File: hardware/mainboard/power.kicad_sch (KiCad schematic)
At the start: 17 parts, among them J105 Eurorack_Power, U1 LM4040DBZ-10, U2 XX1117-3.3

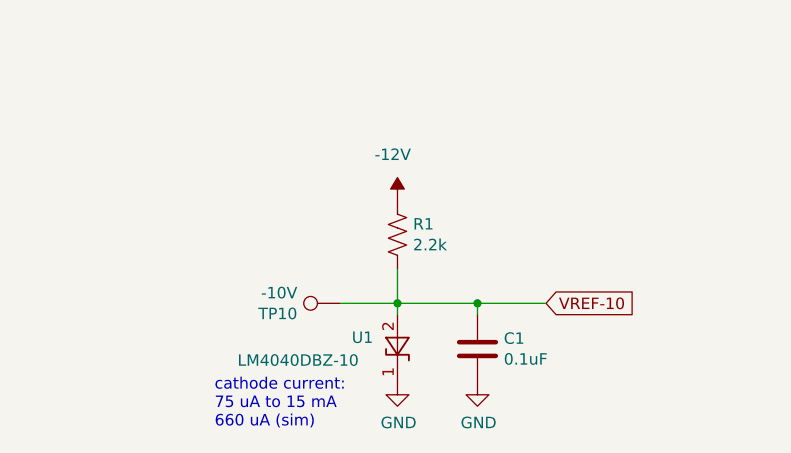
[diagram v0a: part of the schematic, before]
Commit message: Get DRC passing
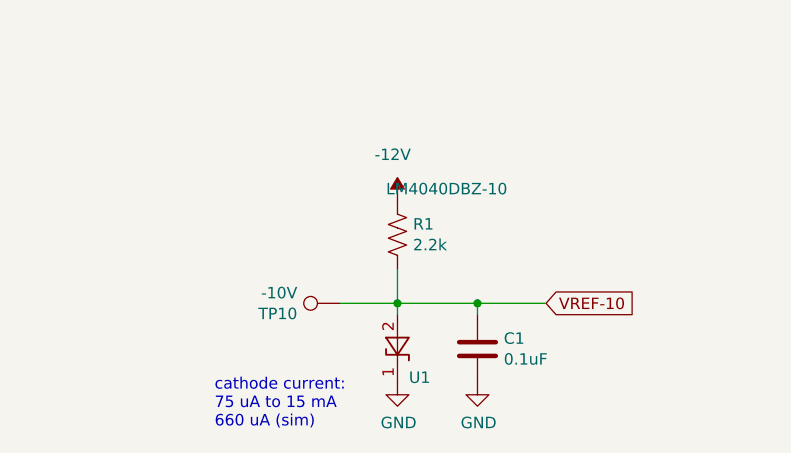
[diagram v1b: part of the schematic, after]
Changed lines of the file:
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@@
   (symbol (lib_id "Reference_Voltage:LM4040DBZ-10") (at 55.88 83.82 270) (unit 1)
     (in_bom yes) (on_board yes)
-    (property "Reference" "U1" (id 0) (at 50.8 82.55 90)
+    (property "Reference" "U1" (id 0) (at 57.15 86.995 90)
       (effects (font (size 1.27 1.27)) (justify left))
     )
-    (property "Value" "LM4040DBZ-10" (id 1) (at 38.1 85.09 90)
+    (property "Value" "LM4040DBZ-10" (id 1) (at 54.61 66.04 90)
       (effects (font (size 1.27 1.27)) (justify left))
     )
-    (property "Footprint" "Package_TO_SOT_SMD:SOT-23" (id 2) (at 50.8 83.82 0)
+    (property "Footprint" "Package_TO_SOT_SMD:SOT-23" (id 2) (at 55.88 78.74 0)
       (effects (font (size 1.27 1.27) italic) hide)
     )
@@
       (effects (font (size 1.27 1.27)) hide)
     )
+    (pin "3")
     (pin "1")
     (pin "2")

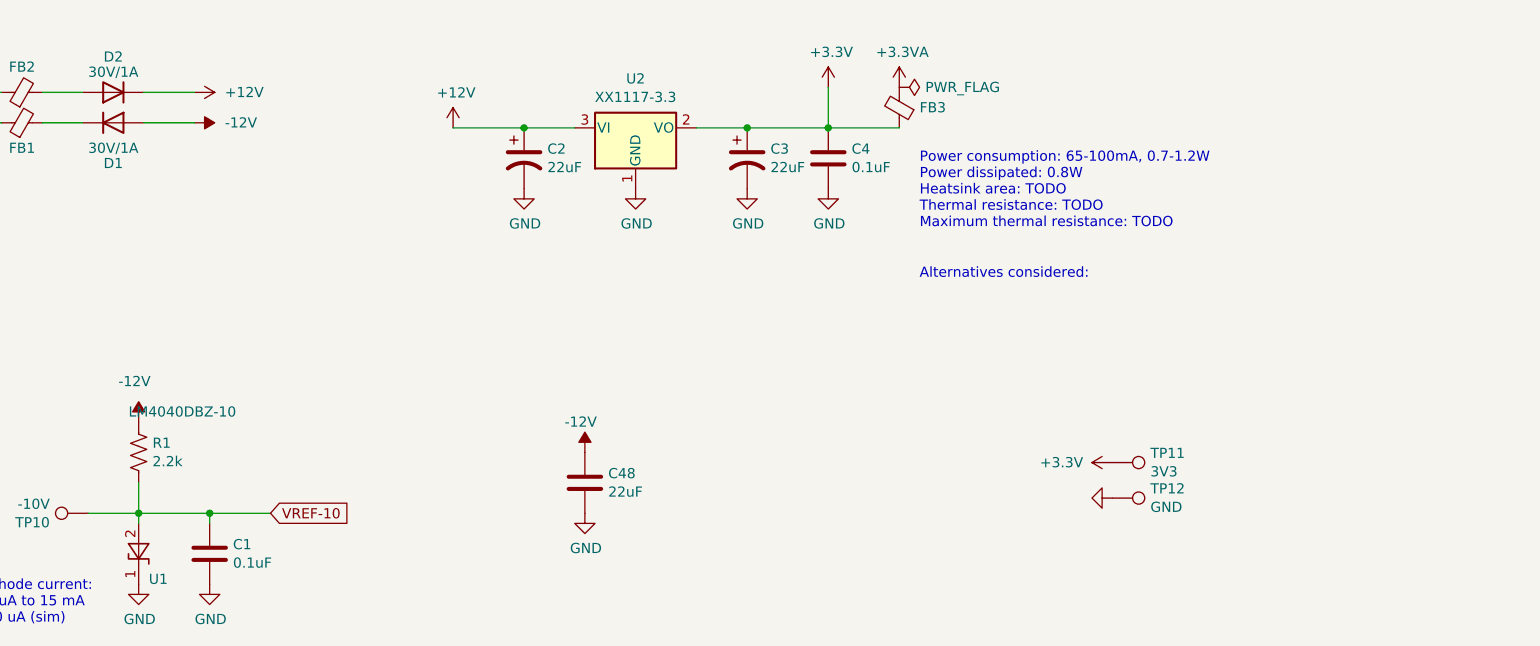
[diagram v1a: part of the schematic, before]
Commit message: Add ESD protection for inputs
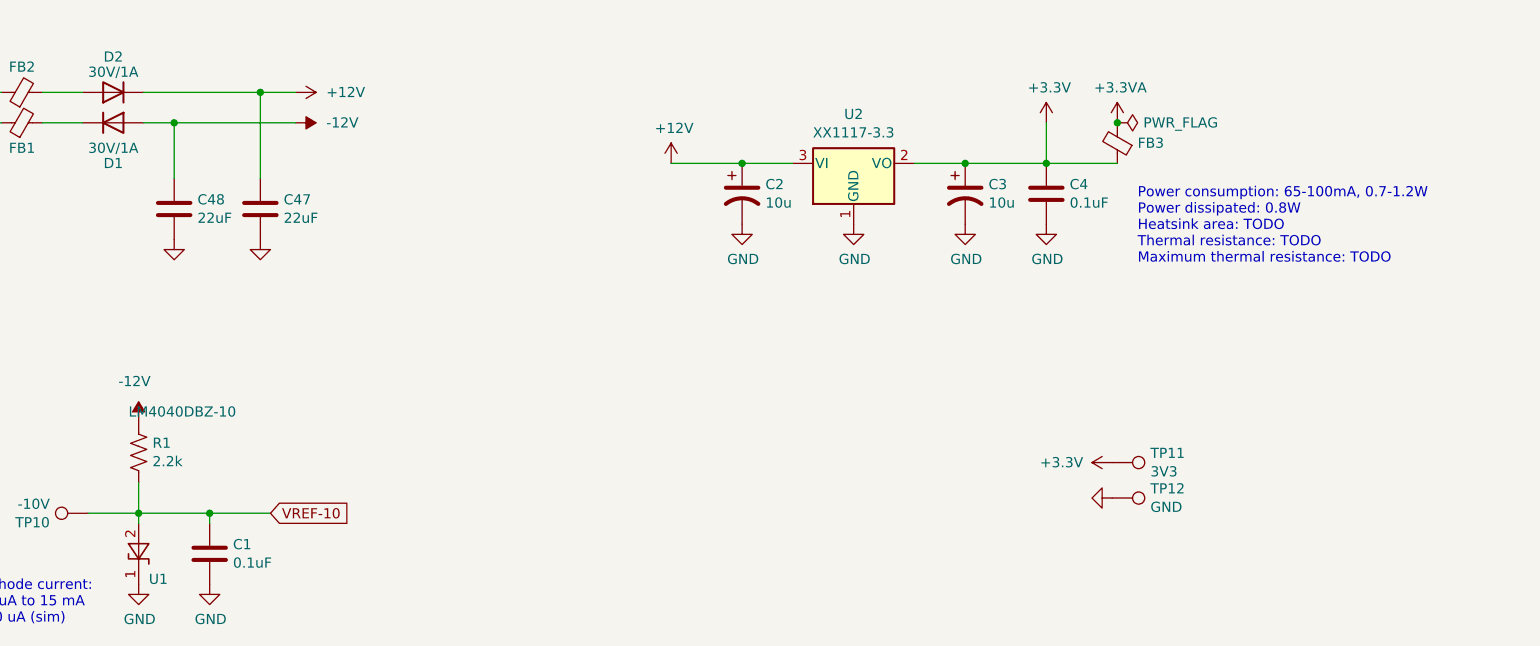
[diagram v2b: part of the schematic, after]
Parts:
- added C47: 22uF, Capacitor_SMD:C_0805_2012Metric_Pad1.18x1.45mm_HandSolder, symbol Device:C
- C2, C3: value 22uF -> 10u; mpn CL21A226MOQNNNE -> (none)
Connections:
- net +12V: now also C47.1
- net GND: now also C47.2
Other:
- note removed: "Alternatives considered:"
- moved on the sheet: C2, C3, C4, C48, FB3, U2

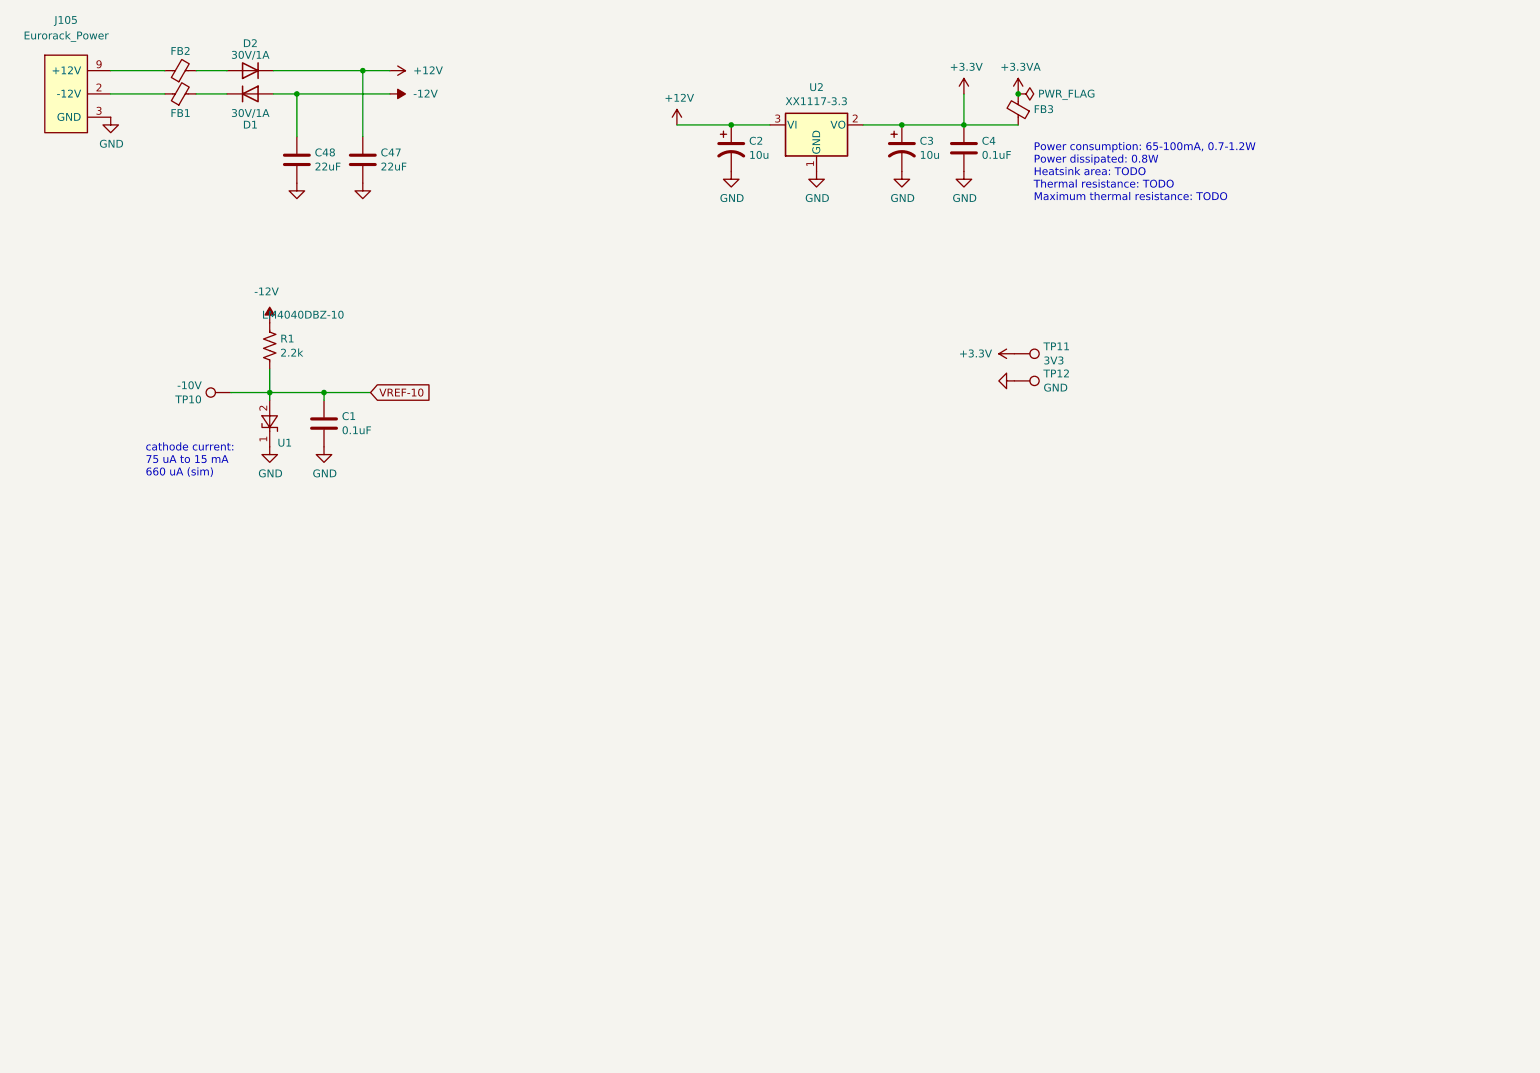
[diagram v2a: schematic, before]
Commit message: Progress on cleaning up the schematics
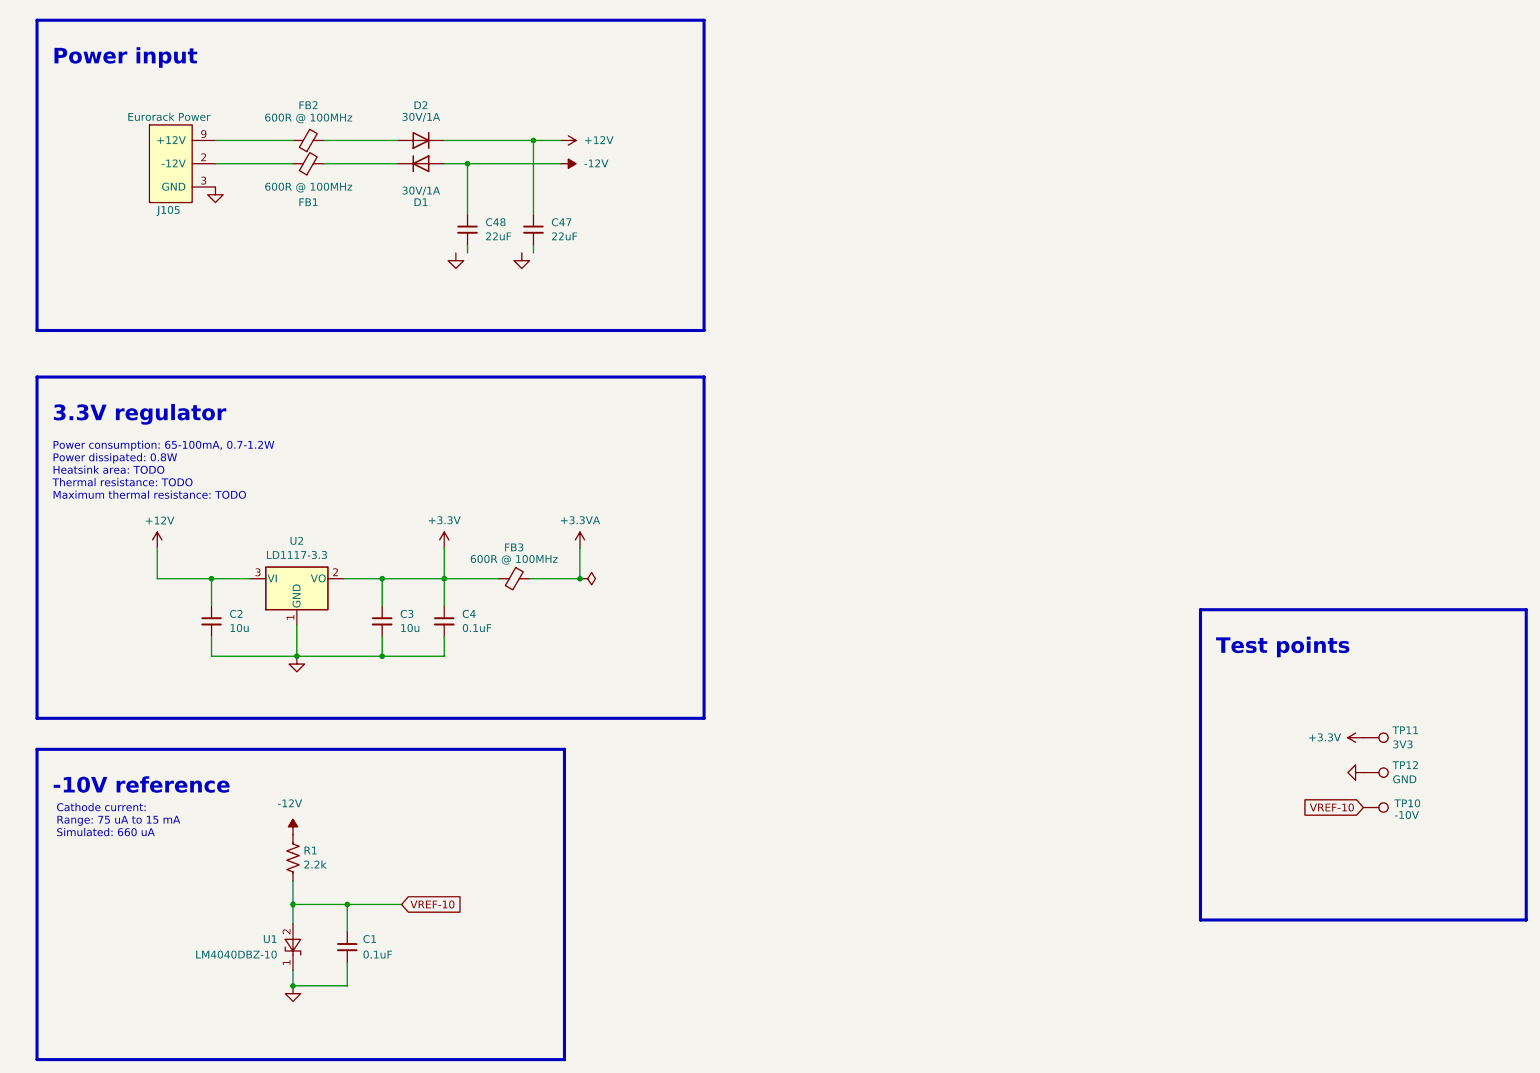
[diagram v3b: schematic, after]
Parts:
- C1, C4, C47, C48: symbol Device:C -> Device:C_Small
- C2, C3: symbol Device:C_Polarized_US -> Device:C_Small
- FB1, FB2: value Ferrite Bead -> 600R @ 100MHz
- FB3: value Ferrite Bead -> 600R @ 100MHz; Reqs >500mA DC current -> >200mA DC current
- J105: value Eurorack_Power -> Eurorack Power
- U2: value XX1117-3.3 -> LD1117-3.3
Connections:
- net +3.3VA: now also FB3.1; no longer FB3.2
- net +3V3: now also FB3.2; no longer FB3.1
- net GND: no longer C47.2, C48.2
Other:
- note added: "-10V reference"
- note added: "3.3V regulator"
- note added: "Cathode current: Range: 75 uA to 15 mA Simulated: 660 uA"
- note added: "Power input"
- note added: "Test points"
- note removed: "cathode current: 75 uA to 15 mA 660 uA (sim)"
- moved on the sheet: C1, C4, C47, C48, D1, D2, FB1, FB2, FB3, J105, R1, TP10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

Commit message: Fixup some wacked stuff from the schematic cleanup
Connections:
- net +3.3VA: now also FB3.2; no longer FB3.1
- net +3V3: now also FB3.1; no longer FB3.2
- net GND: now also C47.2, C48.2
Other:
- moved on the sheet: FB3
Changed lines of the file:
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@@
     (pin "2")
   )
-  (symbol (lib_id "Device:FerriteBead_Small") (at 95.885 109.22 270) (unit 1)
+  (symbol (lib_id "Device:FerriteBead_Small") (at 95.885 109.22 90) (unit 1)
     (in_bom yes) (on_board yes)
     (property "Reference" "FB3" (id 0) (at 95.885 104.14 90))
     (property "Value" "600R @ 100MHz" (id 1) (at 95.885 106.045 90))
-    (property "Footprint" "Inductor_SMD:L_0603_1608Metric_Pad1.05x0.95mm_HandSolder" (id 2) (at 95.885 107.442 90)
+    (property "Footprint" "Inductor_SMD:L_0603_1608Metric_Pad1.05x0.95mm_HandSolder" (id 2) (at 95.885 110.998 90)
       (effects (font (size 1.27 1.27)) hide)
     )
@@
     (pin "2")
   )
-  (symbol (lib_id "power:GND") (at 86.36 55.88 0) (unit 1)
-    (in_bom yes) (on_board yes)
-    (property "Reference" "#PWR02" (id 0) (at 86.36 62.23 0)
-      (effects (font (size 1.27 1.27)) hide)
-    )
-    (property "Value" "GND" (id 1) (at 86.487 60.2742 0)
-      (effects (font (size 1.27 1.27)) hide)
-    )
-    (property "Footprint" "" (id 2) (at 86.36 55.88 0)
-      (effects (font (size 1.27 1.27)) hide)
-    )
-    (property "Datasheet" "" (id 3) (at 86.36 55.88 0)
+  (symbol (lib_id "power:GND") (at 88.265 55.88 0) (unit 1)
+    (in_bom yes) (on_board yes)
+    (property "Reference" "#PWR02" (id 0) (at 88.265 62.23 0)
+      (effects (font (size 1.27 1.27)) hide)
+    )
+    (property "Value" "GND" (id 1) (at 88.392 60.2742 0)
+      (effects (font (size 1.27 1.27)) hide)
+    )
+    (property "Footprint" "" (id 2) (at 88.265 55.88 0)
+      (effects (font (size 1.27 1.27)) hide)
+    )
+    (property "Datasheet" "" (id 3) (at 88.265 55.88 0)
       (effects (font (size 1.27 1.27)) hide)
     )
@@
     (pin "9")
   )
-  (symbol (lib_id "power:GND") (at 97.155 55.88 0) (unit 1)
-    (in_bom yes) (on_board yes)
-    (property "Reference" "#PWR01" (id 0) (at 97.155 62.23 0)
-      (effects (font (size 1.27 1.27)) hide)
-    )
-    (property "Value" "GND" (id 1) (at 97.282 60.2742 0)
-      (effects (font (size 1.27 1.27)) hide)
-    )
-    (property "Footprint" "" (id 2) (at 97.155 55.88 0)
-      (effects (font (size 1.27 1.27)) hide)
-    )
-    (property "Datasheet" "" (id 3) (at 97.155 55.88 0)
-      (effects (font (size 1.27 1.27)) hide)
-    )
+  (symbol (lib_id "power:GND") (at 99.06 55.88 0) (unit 1)
+    (in_bom yes) (on_board yes)
+    (property "Reference" "#PWR01" (id 0) (at 99.06 62.23 0)
+      (effects (font (size 1.27 1.27)) hide)
+    )
+    (property "Value" "GND" (id 1) (at 99.187 60.2742 0)
+      (effects (font (size 1.27 1.27)) hide)
+    )
+    (property "Footprint" "" (id 2) (at 99.06 55.88 0)
+      (effects (font (size 1.27 1.27)) hide)
+    )
+    (property "Datasheet" "" (id 3) (at 99.06 55.88 0)
+      (effects (font (size 1.27 1.27)) hide)
+    )

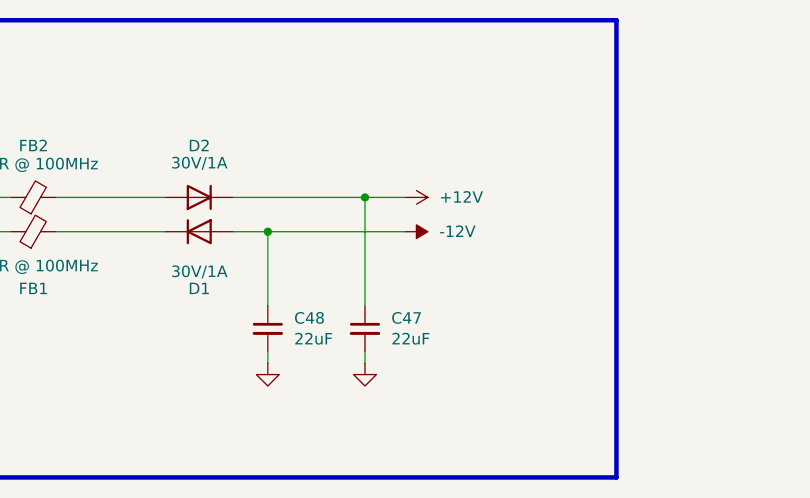
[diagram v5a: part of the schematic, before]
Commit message: Clear ERC
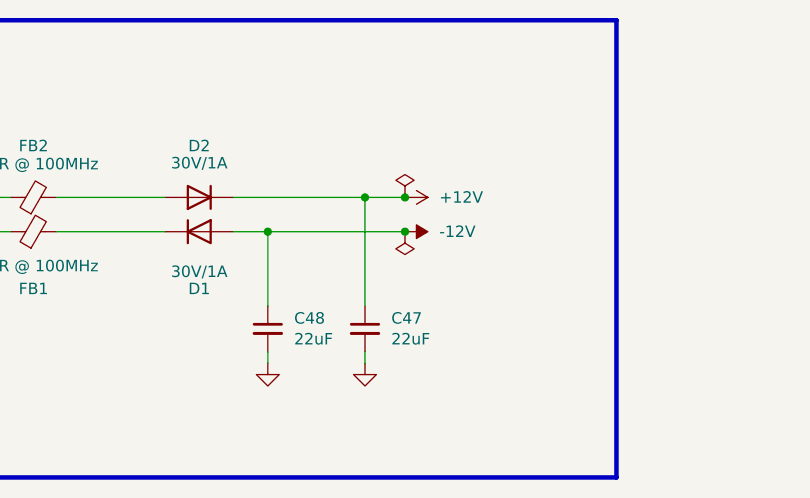
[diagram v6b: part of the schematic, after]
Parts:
- U1: symbol Reference_Voltage:LM4040DBZ-10 -> winterbloom:LM4040DBZ-10
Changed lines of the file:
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@@
   (junction (at 74.295 109.22) (diameter 0) (color 0 0 0 0)
   )
+  (junction (at 103.505 37.465) (diameter 0) (color 0 0 0 0)
+  )
   (junction (at 46.355 109.22) (diameter 0) (color 0 0 0 0)
   )
@@
   )
   (junction (at 74.295 121.92) (diameter 0) (color 0 0 0 0)
+  )
+  (junction (at 103.505 41.275) (diameter 0) (color 0 0 0 0)
   )
   (junction (at 99.06 37.465) (diameter 0) (color 0 0 0 0)
@@
     (pin "2")
   )
-  (symbol (lib_id "Reference_Voltage:LM4040DBZ-10") (at 59.69 169.545 270) (unit 1)
+  (symbol (lib_id "winterbloom:LM4040DBZ-10") (at 59.69 169.545 270) (unit 1)
     (in_bom yes) (on_board yes)
     (property "Reference" "U1" (id 0) (at 57.15 168.275 90)
@@
       (effects (font (size 1.27 1.27)) (justify right))
     )
-    (property "Footprint" "Package_TO_SOT_SMD:SOT-23" (id 2) (at 59.69 164.465 0)
+    (property "Footprint" "Package_TO_SOT_SMD:SOT-23" (id 2) (at 64.77 169.545 0)
       (effects (font (size 1.27 1.27) italic) hide)
     )
@@
     )
     (property "Datasheet" "" (id 3) (at 234.95 135.255 0)
+      (effects (font (size 1.27 1.27)) hide)
+    )
+    (pin "1")
+  )
+  (symbol (lib_id "power:PWR_FLAG") (at 103.505 37.465 0) (unit 1)
+    (in_bom yes) (on_board yes) (fields_autoplaced)
+    (property "Reference" "#FLG01" (id 0) (at 103.505 35.56 0)
+      (effects (font (size 1.27 1.27)) hide)
+    )
+    (property "Value" "PWR_FLAG" (id 1) (at 103.505 31.75 0)
+      (effects (font (size 1.27 1.27)) hide)
+    )
+    (property "Footprint" "" (id 2) (at 103.505 37.465 0)
+      (effects (font (size 1.27 1.27)) hide)
+    )
+    (property "Datasheet" "~" (id 3) (at 103.505 37.465 0)
       (effects (font (size 1.27 1.27)) hide)
     )
@@
       (effects (font (size 1.27 1.27)) hide)
     )
+    (pin "1")
+  )
+  (symbol (lib_id "power:PWR_FLAG") (at 103.505 41.275 180) (unit 1)
+    (in_bom yes) (on_board yes) (fields_autoplaced)
+    (property "Reference" "#FLG02" (id 0) (at 103.505 43.18 0)
+      (effects (font (size 1.27 1.27)) hide)
+    )
+    (property "Value" "PWR_FLAG" (id 1) (at 103.505 46.99 0)
+      (effects (font (size 1.27 1.27)) hide)
+    )
+    (property "Footprint" "" (id 2) (at 103.505 41.275 0)
+      (effects (font (size 1.27 1.27)) hide)
+    )
+    (property "Datasheet" "~" (id 3) (at 103.505 41.275 0)
+      (effects (font (size 1.27 1.27)) hide)
+    )
